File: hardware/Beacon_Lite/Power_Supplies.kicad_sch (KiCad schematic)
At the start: 0 parts

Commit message: Started ST project. Create sch symbols.
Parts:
- added U10, U11, U2: TPS62A02A, symbol Beacon_Lite_Library:TPS62A02A
- added U12: TCR2EF41, symbol Beacon_Lite_Library:TCR2EF41

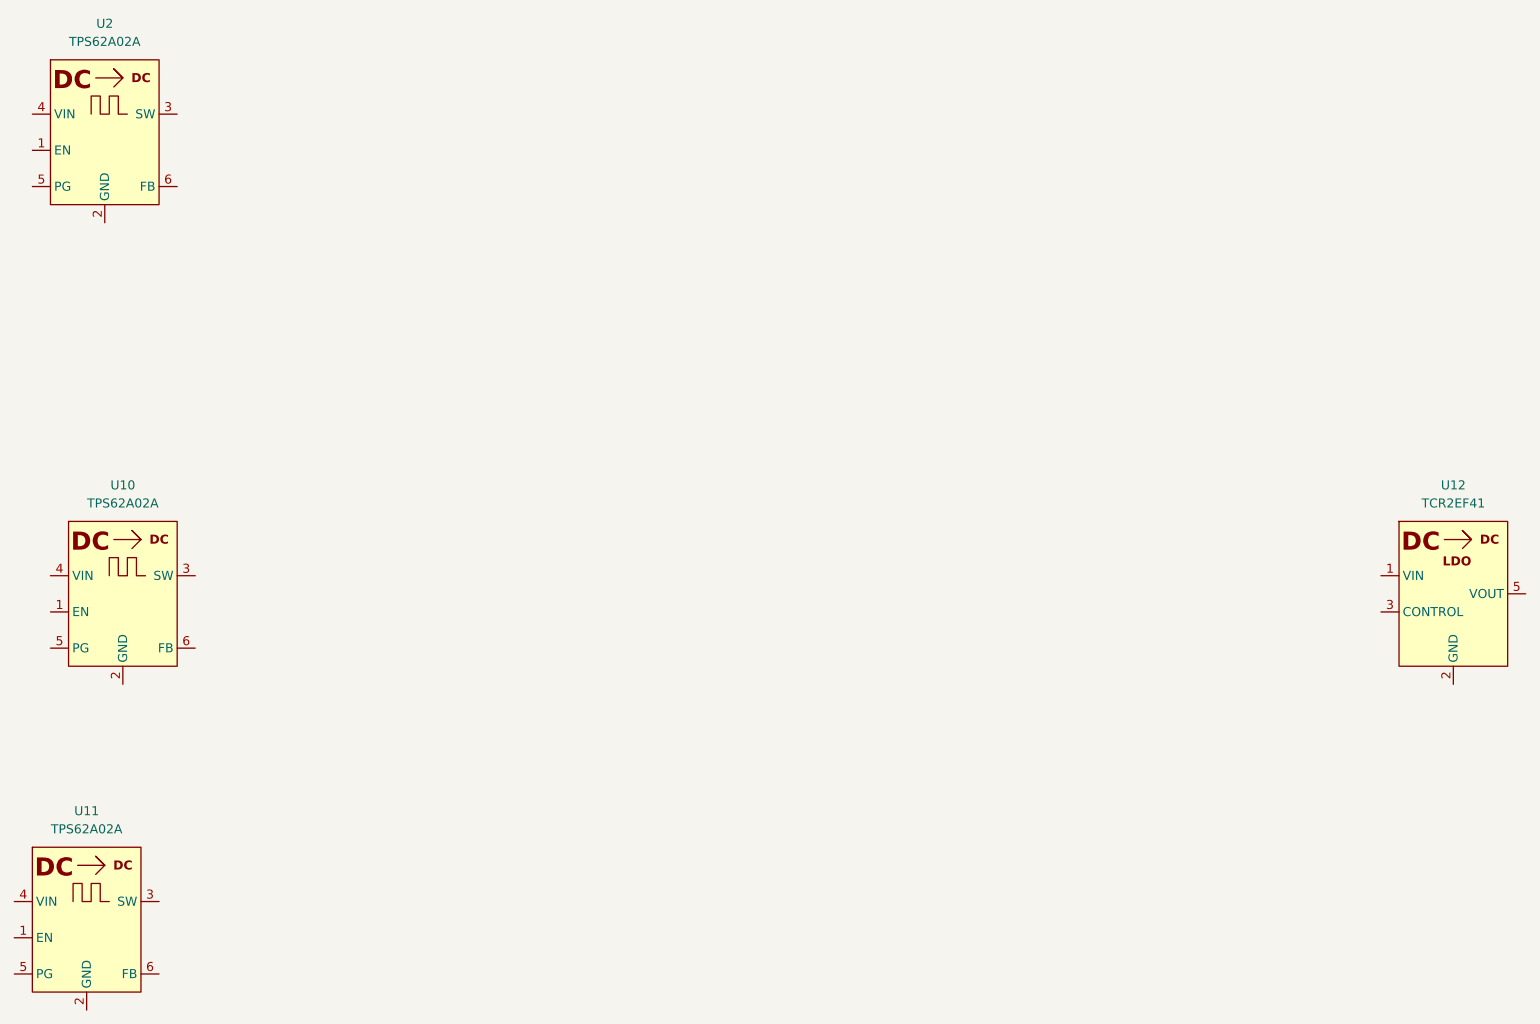
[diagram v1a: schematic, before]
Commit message: Started programming NUCLEO-H533 in VSCODE
* Able to use C++ and C
* Successful able to debug
* Can blink an LED when button is pressed via an interrupt.
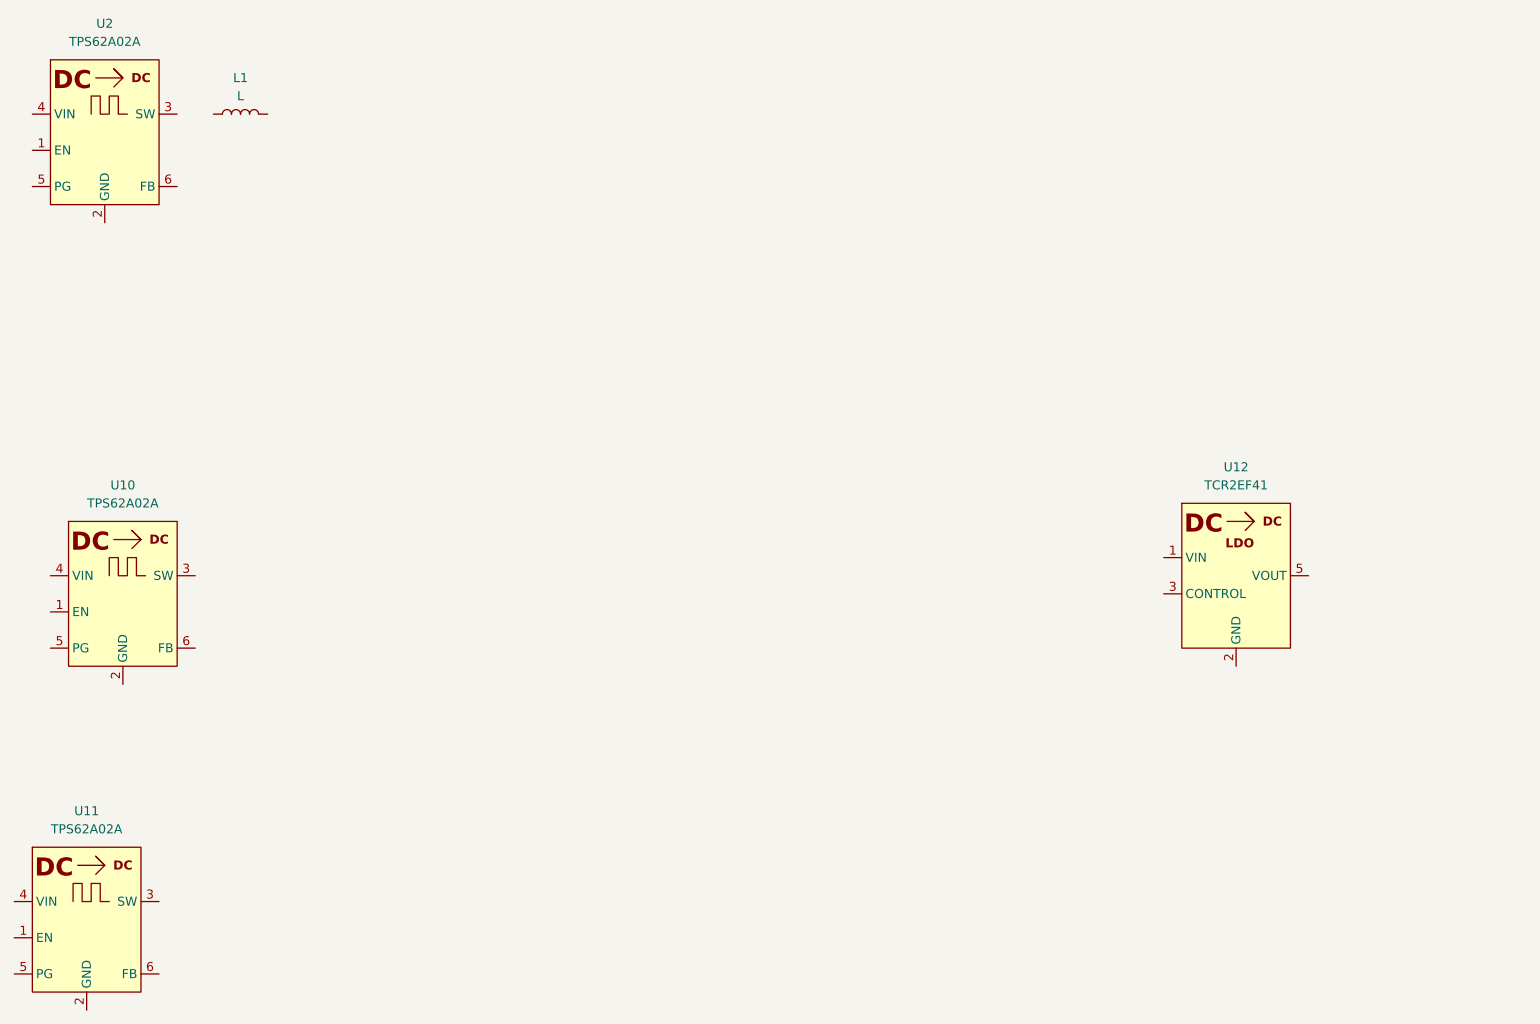
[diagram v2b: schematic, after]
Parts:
- added L1: L, symbol Device:L
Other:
- moved on the sheet: U12
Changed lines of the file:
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@@
 	(symbol
 		(lib_id "Beacon_Lite_Library:TCR2EF41")
-		(at 261.62 104.14 0)
+		(at 231.14 101.6 0)
 		(unit 1)
 		(exclude_from_sim no)
@@
 		(fields_autoplaced yes)
 		(property "Reference" "U12"
-			(at 269.24 99.06 0)
+			(at 238.76 96.52 0)
 			(effects
 				(font
@@
 		)
 		(property "Value" "TCR2EF41"
-			(at 269.24 101.6 0)
+			(at 238.76 99.06 0)
 			(effects
 				(font
@@
 		)
 		(property "Footprint" ""
-			(at 261.62 104.14 0)
+			(at 231.14 101.6 0)
 			(effects
 				(font
@@
 		)
 		(property "Datasheet" "https://www.mouser.com/ProductDetail/Toshiba/TCR2EF41LMCT?qs=cW4DzVrAanNmgIk5awDWSg%3D%3D"
-			(at 261.62 92.456 0)
+			(at 231.14 89.916 0)
 			(effects
 				(font
@@
 		)
 		(property "Description" "LDO, Fixed 4.1Vout, 200mA"
-			(at 268.478 96.012 0)
+			(at 237.998 93.472 0)
 			(effects
 				(font
@@
 					(unit 1)
 				)
+			)
+		)
+	)
+	(symbol
+		(lib_id "Device:L")
+		(at 99.06 46.99 90)
+		(unit 1)
+		(exclude_from_sim no)
+		(in_bom yes)
+		(on_board yes)
+		(dnp no)
+		(fields_autoplaced yes)
+		(property "Reference" "L1"
+			(at 99.06 41.91 90)
+			(effects
+				(font
+					(size 1.27 1.27)
+				)
+			)
+		)
+		(property "Value" "L"
+			(at 99.06 44.45 90)
+			(effects
+				(font
+					(size 1.27 1.27)
+				)
+			)
+		)
+		(property "Footprint" ""
+			(at 99.06 46.99 0)
+			(effects
+				(font
+					(size 1.27 1.27)
+				)
+				(hide yes)
+			)
+		)
+		(property "Datasheet" "~"
+			(at 99.06 46.99 0)
+			(effects
+				(font
+					(size 1.27 1.27)
+				)
+				(hide yes)
+			)
+		)
+		(property "Description" "Inductor"
+			(at 99.06 46.99 0)
+			(effects
+				(font
+					(size 1.27 1.27)
+				)
+				(hide yes)
+			)
+		)
+		(pin "2"
+		)
+		(pin "1"
+		)
+		(instances
+			(project ""
+				(path "/33ebacd6-2d94-4d95-bf8a-b8a1895869c6/77a79242-4d11-452e-8307-dc9047acdfa0"
+					(reference "L1")
+					(unit 1)
+				)
